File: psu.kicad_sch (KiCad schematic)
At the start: 12 parts, among them J1 Power in, J2 Conn_01x02_Male, U2 3.3v REG

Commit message: V3
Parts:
- removed J2: Conn_01x02_Male, Connector_PinHeader_2.54mm:PinHeader_1x02_P2.54mm_Vertical, symbol Connector:Conn_01x02_Male
- removed JP1: SolderJumper_2_Open, Jumper:SolderJumper-2_P1.3mm_Open_RoundedPad1.0x1.5mm, symbol Jumper:SolderJumper_2_Open
- added C14: 220uF 16V, Capacitor_Tantalum_SMD:CP_EIA-7343-31_Kemet-D, symbol Device:C_Polarized
- added C15: 1uF, Capacitor_SMD:C_0402_1005Metric_Pad0.74x0.62mm_HandSolder, symbol Device:C
- C1: value 100nF -> 10uf; footprint Capacitor_SMD:C_0603_1608Metric_Pad1.08x0.95mm_HandSolder -> Capacitor_SMD:C_0402_1005Metric_Pad0.74x0.62mm_HandSolder
- C3: footprint Capacitor_SMD:C_0603_1608Metric_Pad1.08x0.95mm_HandSolder -> Capacitor_SMD:C_0402_1005Metric_Pad0.74x0.62mm_HandSolder
- R1, R2: footprint Resistor_SMD:R_0603_1608Metric_Pad0.98x0.95mm_HandSolder -> Resistor_SMD:R_0402_1005Metric_Pad0.72x0.64mm_HandSolder
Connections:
- net +3V3: now also C15.1
- net +BATT: now also J1.2 (Pin_2)
- net GND: now also C14.2, C15.2
- net VDD: now also C14.1
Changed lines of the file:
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@@
 (kicad_sch (version 20211123) (generator eeschema)
   (paper "A4")
-  (junction (at 43.18 83.82) (diameter 0) (color 0 0 0 0)
-  )
-  (junction (at 45.72 83.82) (diameter 0) (color 0 0 0 0)
+  (junction (at 95.25 39.37) (diameter 0) (color 0 0 0 0)
   )
   (junction (at 50.8 39.37) (diameter 0) (color 0 0 0 0)
@@
   (junction (at 63.5 83.82) (diameter 0) (color 0 0 0 0)
   )
+  (junction (at 67.31 83.82) (diameter 0) (color 0 0 0 0)
+  )
   (junction (at 85.09 39.37) (diameter 0) (color 0 0 0 0)
   )
   (junction (at 50.8 83.82) (diameter 0) (color 0 0 0 0)
   )
-  (wire (pts (xy 40.64 78.74) (xy 40.64 81.28))
-    (stroke (width 0) (type default) (color 0 0 0 0))
-  )
-  (wire (pts (xy 40.64 81.28) (xy 43.18 81.28))
-    (stroke (width 0) (type default) (color 0 0 0 0))
-  )
   (wire (pts (xy 50.8 39.37) (xy 59.69 39.37))
     (stroke (width 0) (type default) (color 0 0 0 0))
   )
-  (wire (pts (xy 45.72 81.28) (xy 48.26 81.28))
-    (stroke (width 0) (type default) (color 0 0 0 0))
-  )
-  (wire (pts (xy 36.83 83.82) (xy 43.18 83.82))
-    (stroke (width 0) (type default) (color 0 0 0 0))
-  )
-  (wire (pts (xy 43.18 81.28) (xy 43.18 83.82))
-    (stroke (width 0) (type default) (color 0 0 0 0))
-  )
-  (wire (pts (xy 48.26 81.28) (xy 48.26 78.74))
+  (wire (pts (xy 85.09 39.37) (xy 95.25 39.37))
     (stroke (width 0) (type default) (color 0 0 0 0))
   )
@@
     (stroke (width 0) (type default) (color 0 0 0 0))
   )
-  (wire (pts (xy 45.72 83.82) (xy 50.8 83.82))
-    (stroke (width 0) (type default) (color 0 0 0 0))
-  )
-  (wire (pts (xy 45.72 83.82) (xy 45.72 81.28))
+  (wire (pts (xy 36.83 83.82) (xy 50.8 83.82))
     (stroke (width 0) (type default) (color 0 0 0 0))
   )
@@
     (pin "1")
   )
-  (symbol (lib_id "power:+3.3V") (at 85.09 39.37 0) (unit 1)
-    (in_bom yes) (on_board yes) (fields_autoplaced)
-    (property "Reference" "#PWR0105" (id 0) (at 85.09 43.18 0)
-      (effects (font (size 1.27 1.27)) hide)
-    )
-    (property "Value" "+3.3V" (id 1) (at 85.09 34.29 0))
-    (property "Footprint" "" (id 2) (at 85.09 39.37 0)
-      (effects (font (size 1.27 1.27)) hide)
-    )
-    (property "Datasheet" "" (id 3) (at 85.09 39.37 0)
+  (symbol (lib_id "power:+3.3V") (at 95.25 39.37 0) (unit 1)
+    (in_bom yes) (on_board yes) (fields_autoplaced)
+    (property "Reference" "#PWR0105" (id 0) (at 95.25 43.18 0)
+      (effects (font (size 1.27 1.27)) hide)
+    )
+    (property "Value" "+3.3V" (id 1) (at 95.25 34.29 0))
+    (property "Footprint" "" (id 2) (at 95.25 39.37 0)
+      (effects (font (size 1.27 1.27)) hide)
+    )
+    (property "Datasheet" "" (id 3) (at 95.25 39.37 0)
       (effects (font (size 1.27 1.27)) hide)
     )
@@
       (effects (font (size 1.27 1.27)) (justify left))
     )
-    (property "Value" "100nF" (id 1) (at 54.61 45.72 0)
-      (effects (font (size 1.27 1.27)) (justify left))
-    )
-    (property "Footprint" "Capacitor_SMD:C_0603_1608Metric_Pad1.08x0.95mm_HandSolder" (id 2) (at 51.7652 46.99 0)
+    (property "Value" "10uf" (id 1) (at 54.61 45.72 0)
+      (effects (font (size 1.27 1.27)) (justify left))
+    )
+    (property "Footprint" "Capacitor_SMD:C_0402_1005Metric_Pad0.74x0.62mm_HandSolder" (id 2) (at 51.7652 46.99 0)
       (effects (font (size 1.27 1.27)) hide)
     )
@@
     (pin "2")
   )
-  (symbol (lib_id "Connector:Conn_01x02_Male") (at 43.18 88.9 90) (unit 1)
-    (in_bom yes) (on_board yes) (fields_autoplaced)
-    (property "Reference" "J2" (id 0) (at 46.99 86.9949 90)
-      (effects (font (size 1.27 1.27)) (justify right))
-    )
-    (property "Value" "Conn_01x02_Male" (id 1) (at 46.99 89.5349 90)
-      (effects (font (size 1.27 1.27)) (justify right) hide)
-    )
-    (property "Footprint" "Connector_PinHeader_2.54mm:PinHeader_1x02_P2.54mm_Vertical" (id 2) (at 43.18 88.9 0)
-      (effects (font (size 1.27 1.27)) hide)
-    )
-    (property "Datasheet" "~" (id 3) (at 43.18 88.9 0)
-      (effects (font (size 1.27 1.27)) hide)
-    )
-    (pin "1")
-    (pin "2")
-  )
   (symbol (lib_id "power:GND") (at 85.09 46.99 0) (unit 1)
     (in_bom yes) (on_board yes) (fields_autoplaced)
@@
     (pin "1")
   )
+  (symbol (lib_id "Device:C_Polarized") (at 67.31 87.63 0) (unit 1)
+    (in_bom yes) (on_board yes) (fields_autoplaced)
+    (property "Reference" "C14" (id 0) (at 70.485 85.4709 0)
+      (effects (font (size 1.27 1.27)) (justify left))
+    )
+    (property "Value" "220uF 16V" (id 1) (at 70.485 88.0109 0)
+      (effects (font (size 1.27 1.27)) (justify left))
+    )
+    (property "Footprint" "Capacitor_Tantalum_SMD:CP_EIA-7343-31_Kemet-D" (id 2) (at 68.2752 91.44 0)
+      (effects (font (size 1.27 1.27)) hide)
+    )
+    (property "Datasheet" "~" (id 3) (at 67.31 87.63 0)
+      (effects (font (size 1.27 1.27)) hide)
+    )
+    (pin "1")
+    (pin "2")
+  )
   (symbol (lib_id "power:+3.3V") (at 35.56 34.29 0) (unit 1)
     (in_bom yes) (on_board yes)
@@
     (pin "1")
   )
+  (symbol (lib_id "power:GND") (at 67.31 91.44 0) (unit 1)
+    (in_bom yes) (on_board yes) (fields_autoplaced)
+    (property "Reference" "#PWR0117" (id 0) (at 67.31 97.79 0)
+      (effects (font (size 1.27 1.27)) hide)
+    )
+    (property "Value" "GND" (id 1) (at 67.31 96.52 0))
+    (property "Footprint" "" (id 2) (at 67.31 91.44 0)
+      (effects (font (size 1.27 1.27)) hide)
+    )
+    (property "Datasheet" "" (id 3) (at 67.31 91.44 0)
+      (effects (font (size 1.27 1.27)) hide)
+    )
+    (pin "1")
+  )
   (symbol (lib_id "power:GND") (at 50.8 46.99 0) (unit 1)
     (in_bom yes) (on_board yes) (fields_autoplaced)
@@
     (property "Reference" "R1" (id 0) (at 22.86 46.99 90))
     (property "Value" "22k" (id 1) (at 27.94 46.99 90))
-    (property "Footprint" "Resistor_SMD:R_0603_1608Metric_Pad0.98x0.95mm_HandSolder" (id 2) (at 23.622 45.72 90)
+    (property "Footprint" "Resistor_SMD:R_0402_1005Metric_Pad0.72x0.64mm_HandSolder" (id 2) (at 23.622 45.72 90)
       (effects (font (size 1.27 1.27)) hide)
     )
@@
       (effects (font (size 1.27 1.27)) (justify left))
     )
-    (property "Value" "10uF" (id 1) (at 78.74 44.45 0)
-      (effects (font (size 1.27 1.27)) (justify left))
-    )
-    (property "Footprint" "Capacitor_SMD:C_0603_1608Metric_Pad1.08x0.95mm_HandSolder" (id 2) (at 86.0552 46.99 0)
+    (property "Value" "10uF" (id 1) (at 77.47 45.72 0)
+      (effects (font (size 1.27 1.27)) (justify left))
+    )
+    (property "Footprint" "Capacitor_SMD:C_0402_1005Metric_Pad0.74x0.62mm_HandSolder" (id 2) (at 86.0552 46.99 0)
       (effects (font (size 1.27 1.27)) hide)
     )
@@
     (pin "1")
   )
+  (symbol (lib_id "Device:C") (at 95.25 43.18 0) (unit 1)
+    (in_bom yes) (on_board yes)
+    (property "Reference" "C15" (id 0) (at 90.17 43.18 0)
+      (effects (font (size 1.27 1.27)) (justify left))
+    )
+    (property "Value" "1uF" (id 1) (at 88.9 45.72 0)
+      (effects (font (size 1.27 1.27)) (justify left))
+    )
+    (property "Footprint" "Capacitor_SMD:C_0402_1005Metric_Pad0.74x0.62mm_HandSolder" (id 2) (at 96.2152 46.99 0)
+      (effects (font (size 1.27 1.27)) hide)
+    )
+    (property "Datasheet" "~" (id 3) (at 95.25 43.18 0)
+      (effects (font (size 1.27 1.27)) hide)
+    )
+    (pin "1")
+    (pin "2")
+  )
   (symbol (lib_id "Device:R") (at 35.56 45.72 0) (unit 1)
     (in_bom yes) (on_board yes)
     (property "Reference" "R2" (id 0) (at 33.02 46.99 90))
     (property "Value" "10k" (id 1) (at 38.1 46.99 90))
-    (property "Footprint" "Resistor_SMD:R_0603_1608Metric_Pad0.98x0.95mm_HandSolder" (id 2) (at 33.782 45.72 90)
+    (property "Footprint" "Resistor_SMD:R_0402_1005Metric_Pad0.72x0.64mm_HandSolder" (id 2) (at 33.782 45.72 90)
       (effects (font (size 1.27 1.27)) hide)
     )
     (property "Datasheet" "~" (id 3) (at 35.56 45.72 0)
-      (effects (font (size 1.27 1.27)) hide)
-    )
-    (pin "1")
-    (pin "2")
-  )
-  (symbol (lib_id "Jumper:SolderJumper_2_Open") (at 44.45 78.74 0) (unit 1)
-    (in_bom yes) (on_board yes) (fields_autoplaced)
-    (property "Reference" "JP1" (id 0) (at 44.45 72.39 0))
-    (property "Value" "SolderJumper_2_Open" (id 1) (at 44.45 74.93 0)
-      (effects (font (size 1.27 1.27)) hide)
-    )
-    (property "Footprint" "Jumper:SolderJumper-2_P1.3mm_Open_RoundedPad1.0x1.5mm" (id 2) (at 44.45 78.74 0)
-      (effects (font (size 1.27 1.27)) hide)
-    )
-    (property "Datasheet" "~" (id 3) (at 44.45 78.74 0)
       (effects (font (size 1.27 1.27)) hide)
     )
@@
       (effects (font (size 1.27 1.27)) hide)
     )
+    (pin "1")
+  )
+  (symbol (lib_id "power:GND") (at 95.25 46.99 0) (unit 1)
+    (in_bom yes) (on_board yes) (fields_autoplaced)
+    (property "Reference" "#PWR0142" (id 0) (at 95.25 53.34 0)
+      (effects (font (size 1.27 1.27)) hide)
+    )
+    (property "Value" "GND" (id 1) (at 95.25 52.07 0))
+    (property "Footprint" "" (id 2) (at 95.25 46.99 0)
+      (effects (font (size 1.27 1.27)) hide)
+    )
+    (property "Datasheet" "" (id 3) (at 95.25 46.99 0)
+      (effects (font (size 1.27 1.27)) hide)
+    )

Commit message: Rev 27052023
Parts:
- removed C1: 10uf, Capacitor_SMD:C_0402_1005Metric_Pad0.74x0.62mm_HandSolder, symbol Device:C
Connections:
- net VDD is gone; now on net GND: C14.1, D1.2 (A), D3.1 (K), D4.1 (K), U2.3 (VI)
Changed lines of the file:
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@@
   (junction (at 50.8 83.82) (diameter 0) (color 0 0 0 0)
+  )
+  (wire (pts (xy 50.8 39.37) (xy 50.8 46.99))
+    (stroke (width 0) (type default) (color 0 0 0 0))
   )
   (wire (pts (xy 50.8 39.37) (xy 59.69 39.37))
@@
       (effects (font (size 1.27 1.27)) hide)
     )
-    (pin "1")
-    (pin "2")
-  )
-  (symbol (lib_id "Device:C") (at 50.8 43.18 0) (unit 1)
-    (in_bom yes) (on_board yes)
-    (property "Reference" "C1" (id 0) (at 54.61 43.18 0)
-      (effects (font (size 1.27 1.27)) (justify left))
-    )
-    (property "Value" "10uf" (id 1) (at 54.61 45.72 0)
-      (effects (font (size 1.27 1.27)) (justify left))
-    )
-    (property "Footprint" "Capacitor_SMD:C_0402_1005Metric_Pad0.74x0.62mm_HandSolder" (id 2) (at 51.7652 46.99 0)
-      (effects (font (size 1.27 1.27)) hide)
-    )
-    (property "Datasheet" "~" (id 3) (at 50.8 43.18 0)
-      (effects (font (size 1.27 1.27)) hide)
-    )

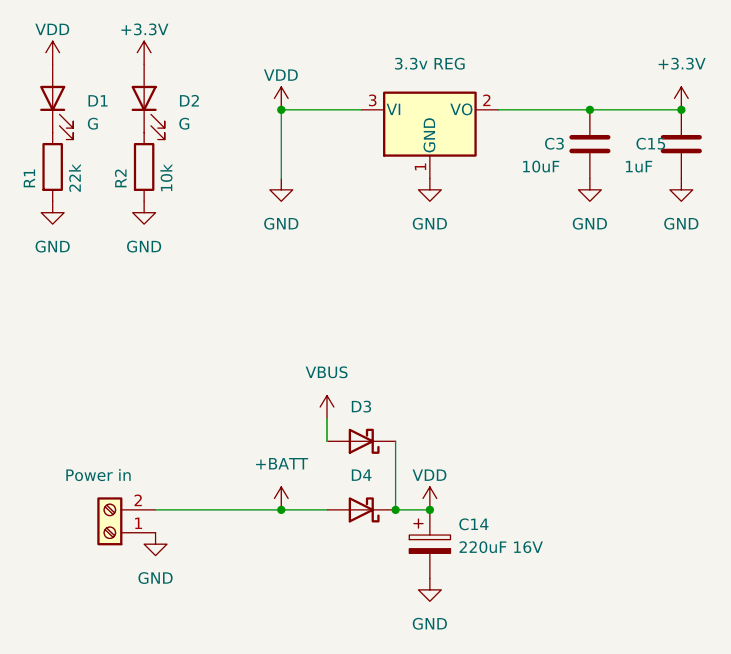
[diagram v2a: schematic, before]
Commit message: fixed ground short
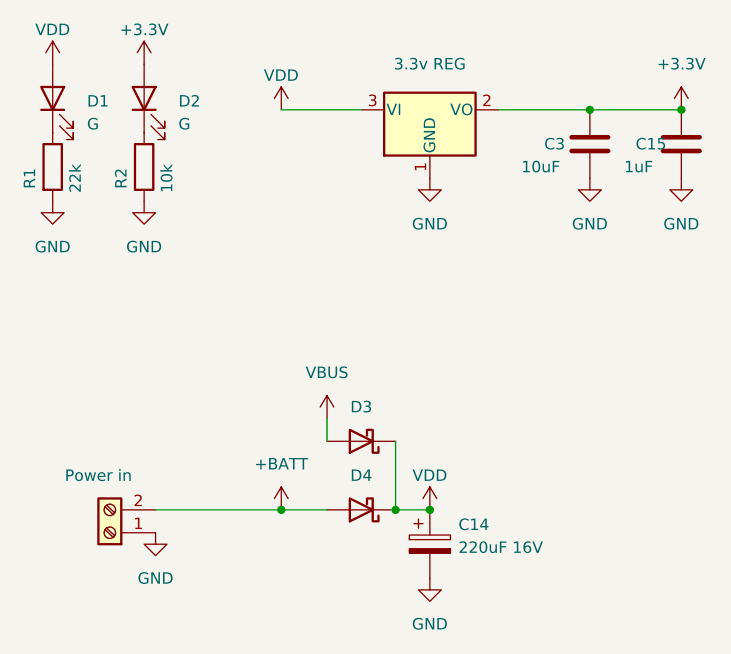
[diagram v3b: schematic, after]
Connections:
- net GND: no longer C14.1, D1.2 (A), D3.1 (K), D4.1 (K), U2.3 (VI)
- new net VDD: C14.1, D1.2 (A), D3.1 (K), D4.1 (K), U2.3 (VI)
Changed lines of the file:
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@@
   (junction (at 95.25 39.37) (diameter 0) (color 0 0 0 0)
   )
-  (junction (at 50.8 39.37) (diameter 0) (color 0 0 0 0)
-  )
   (junction (at 63.5 83.82) (diameter 0) (color 0 0 0 0)
   )
@@
   )
   (junction (at 50.8 83.82) (diameter 0) (color 0 0 0 0)
-  )
-  (wire (pts (xy 50.8 39.37) (xy 50.8 46.99))
-    (stroke (width 0) (type default) (color 0 0 0 0))
   )
   (wire (pts (xy 50.8 39.37) (xy 59.69 39.37))
@@
       (effects (font (size 1.27 1.27)) hide)
     )
-    (pin "1")
-  )
-  (symbol (lib_id "power:GND") (at 50.8 46.99 0) (unit 1)
-    (in_bom yes) (on_board yes) (fields_autoplaced)
-    (property "Reference" "#PWR0106" (id 0) (at 50.8 53.34 0)
-      (effects (font (size 1.27 1.27)) hide)
-    )
-    (property "Value" "GND" (id 1) (at 50.8 52.07 0))
-    (property "Footprint" "" (id 2) (at 50.8 46.99 0)
-      (effects (font (size 1.27 1.27)) hide)
-    )
-    (property "Datasheet" "" (id 3) (at 50.8 46.99 0)
-      (effects (font (size 1.27 1.27)) hide)
-    )
